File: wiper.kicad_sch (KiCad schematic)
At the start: 63 parts, among them J1 Conn_01x02, J10 Conn_01x02, J2 Sensor FW, J3 Sensor BK, J4 Conn_01x02, J5 Conn_01x02, J6 PROG, J7 I2C, J8 UART, J9 Conn_01x02, K1 G5LE-1, K2 G5LE-1, Q1 MMBT2222A, Q2 MMBT2222A, Q3 MMBT2222A, Q4 MMBT2222A, SW1 Reset, U1 LM7805_TO220, U2 PC817, U3 PC817, U4 KA78M05_TO252, U5 ATmega48-20A, Y1 16MHz

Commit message: v1.0: version sent to production (2026-02-11)
PCB matches the Gerber files generated 2026-02-11 18:12.
- Add potentiometer RV1 (10K) and capacitor C10 (100nF)
- Remove test point TP1
- Replace M3 ISO7380 mounting holes with M3
- Complete PCB routing

Schematic restored to its state at production time:
C7 = 100nF, matching the PCB.

Co-Authored-By: Claude Opus 5.5 <noreply@anthropic.com>
Claude-Session: https://claude.ai/code/session_01ADaCdURCPQ1EkJMwDbARyU
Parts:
- removed TP1: ~, Connector_PinHeader_1.00mm:PinHeader_1x01_P1.00mm_Vertical, symbol Connector:TestPoint
- added C10: 100nF, Resistor_SMD:R_0603_1608Metric_Pad0.98x0.95mm_HandSolder, symbol Device:C_Small
- added RV1: 10K, Potentiometer_THT:Potentiometer_ACP_CA9-V10_Vertical, symbol Device:R_Potentiometer
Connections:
- net +5V: now also C10.1, RV1.1
- net at U5.19 (ADC6): now also RV1.2
- new net: C10.2, RV1.3
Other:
- note added: "WIPER 2.2"
- note removed: "WIPER 2.1"

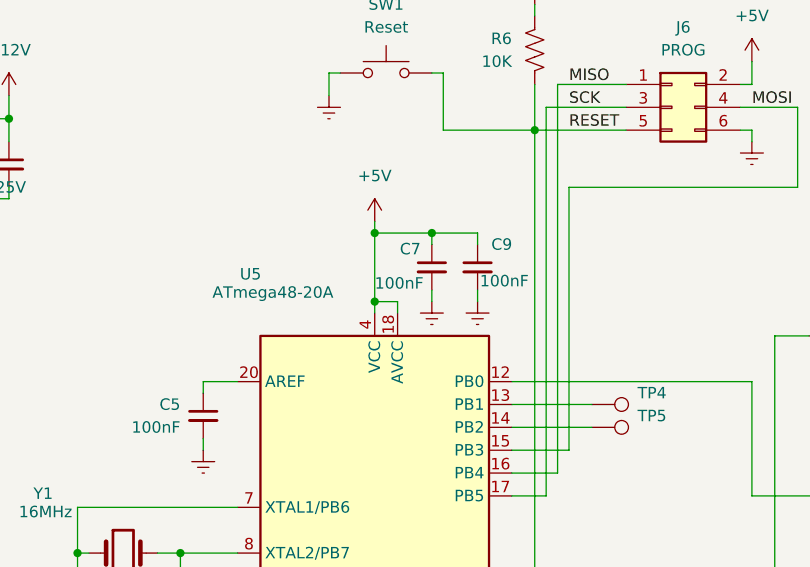
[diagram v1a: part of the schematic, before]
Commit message: Start v2: change C7 to 10uF in schematic
Not yet applied to the PCB (run Update PCB from Schematic, F8).

Co-Authored-By: Claude Opus 5.5 <noreply@anthropic.com>
Claude-Session: https://claude.ai/code/session_01ADaCdURCPQ1EkJMwDbARyU
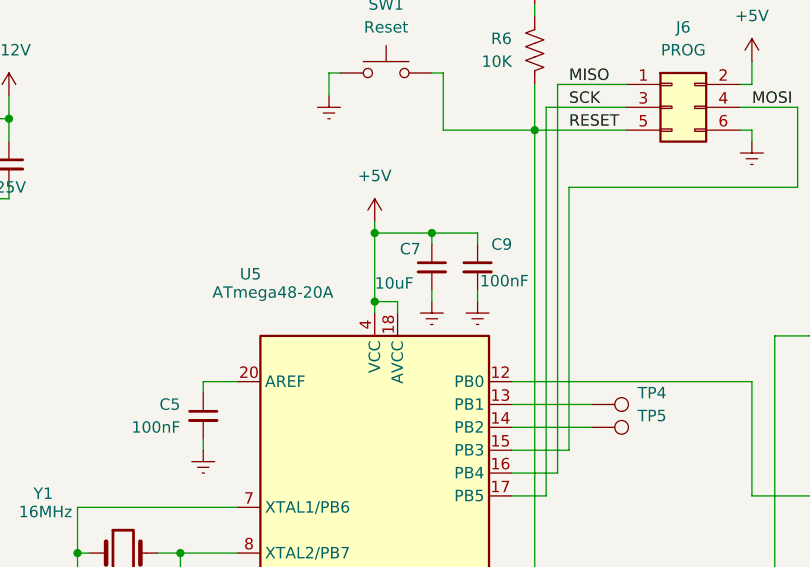
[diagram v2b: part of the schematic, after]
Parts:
- C7: value 100nF -> 10uF
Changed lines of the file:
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@@
 			)
 		)
-		(property "Value" "100nF"
+		(property "Value" "10uF"
 			(at 97.79 50.038 0)
 			(effects
